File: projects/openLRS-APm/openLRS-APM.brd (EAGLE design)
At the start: 43.3 x 21.8 mm, 23 parts, among them IC2 RFM23BPSMD, J1 AVR_SPI_PRG_6PTH, U1 ATMEGA328P, X2 SMA-142-0711-821/826, Y1 16MHz

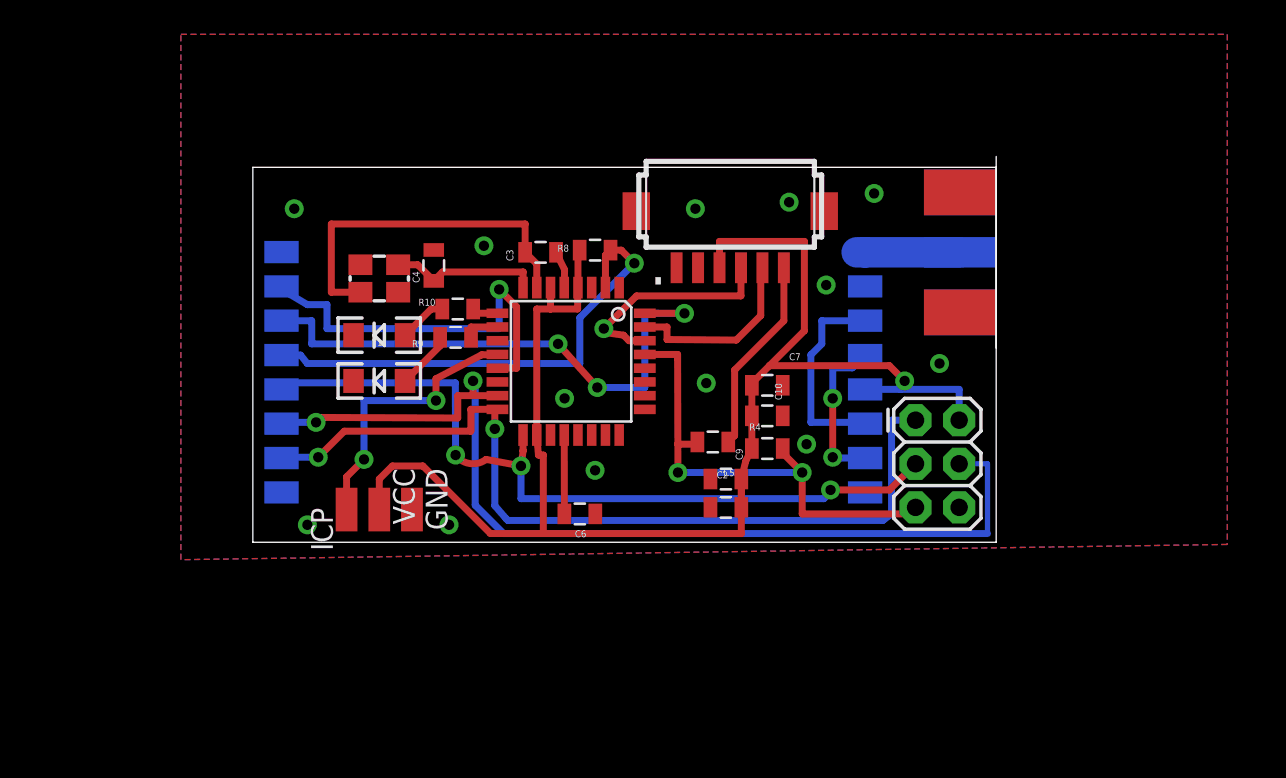
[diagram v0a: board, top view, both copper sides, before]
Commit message: Fixed designs
Ready for first fabrication (I hope). Cleaned and prepared.
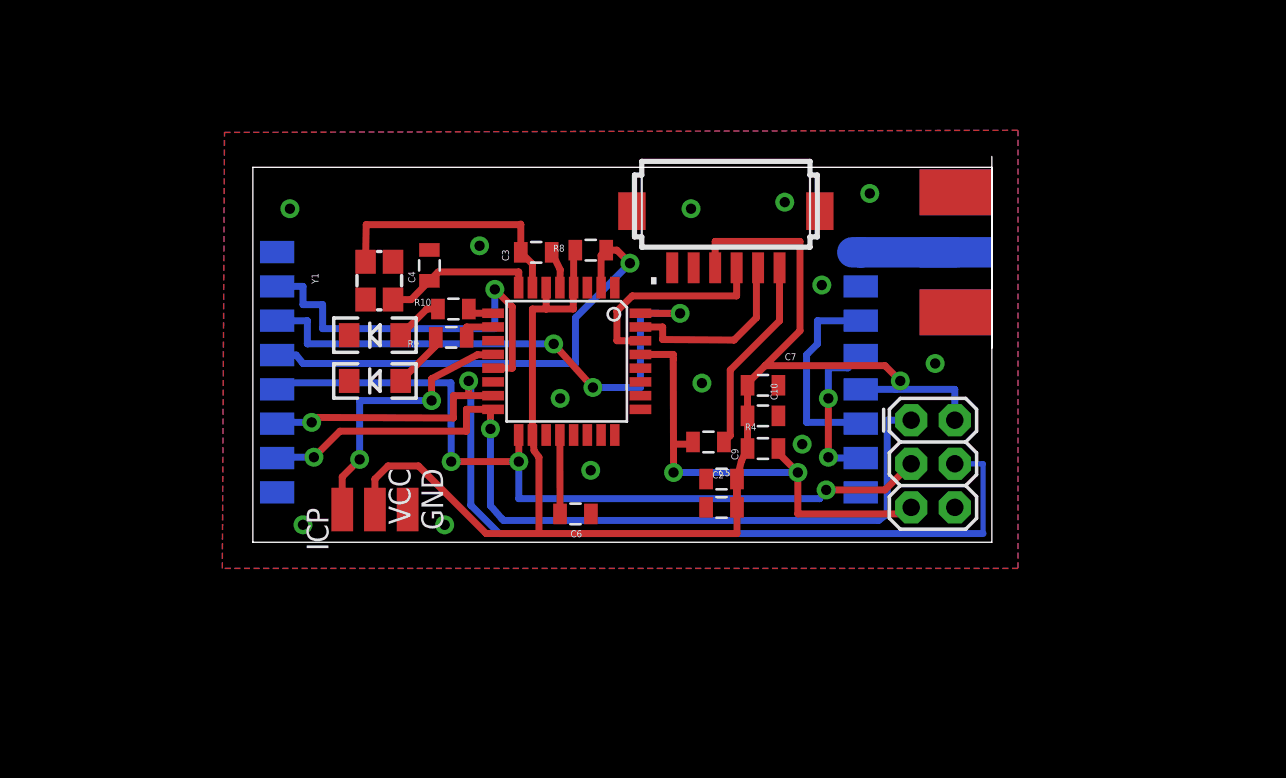
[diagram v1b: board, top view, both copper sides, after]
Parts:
- moved X2 0.25 mm to (43.1, 16.9)
- moved C10 0.25 mm to (29.7, 7.37)
- moved C2 0.25 mm to (27.3, 2.03)
- moved C5 0.25 mm to (26.5, 5.84)
- moved C6 0.25 mm to (18.8, 1.65)
- moved C7 0.25 mm to (29.7, 9.14)
- moved C9 0.25 mm to (27.3, 3.68)
- moved GND 0.25 mm to (9.02, 1.91)
- moved IC2 0.25 mm to (18.4, 9.91)
- moved R10 0.25 mm to (11.7, 13.6)
- moved R4 0.25 mm to (29.7, 5.46)
- moved R8 0.25 mm to (19.7, 17.0)
- moved U1 0.25 mm to (18.3, 10.5)
- moved ICP 0.25 mm to (5.21, 1.91)
- moved C4 0.25 mm to (10.3, 16.1)
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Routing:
- net N$11: track 21.0 -> 15.2 mm
- net RXD: track 13.1 -> 12.1 mm, vias 1 -> 0
- net SDN: track 22.9 -> 23.7 mm
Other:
- board size 43.3 x 21.8 mm -> 43.1 x 21.8 mm

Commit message: Cleaned, Checked, fixed Ground planes
Beefed up Power busses. Fixed the Telemetry Pinout.
Closer to a polished Revision one. Will look into DF-13 PPM signals.
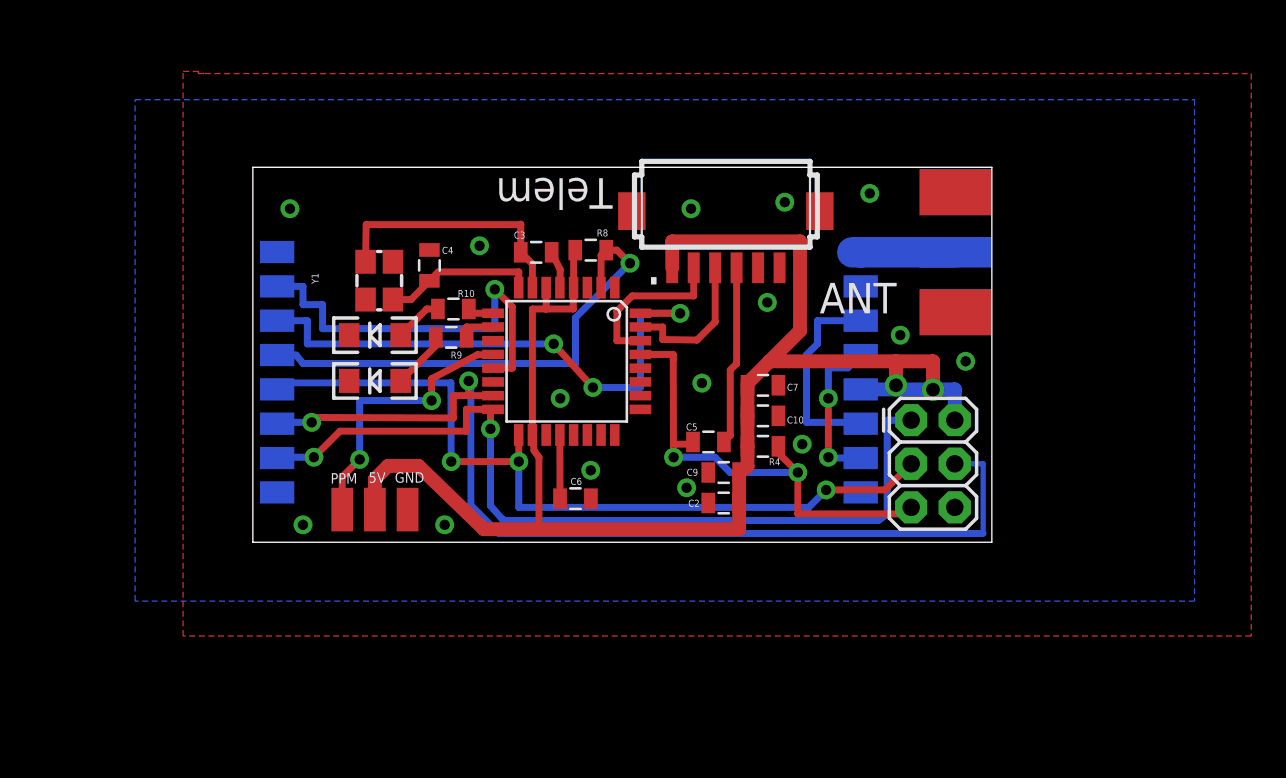
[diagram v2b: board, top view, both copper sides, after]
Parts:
- moved C6 0.89 mm to (18.8, 2.54)
- moved C9 0.40 mm to (27.4, 4.06)
- moved C2 0.28 mm to (27.4, 2.29)
- moved R4 0.13 mm to (29.7, 5.59)
- renumbered ICP to PPM, VCC to 5V
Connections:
- net ICP renamed PPM
- removed net SCL: U1.28
- removed net SDA: U1.27
- removed net VCN: U1.11
- net DTR: now also TELEMETRY.P$4; no longer TELEMETRY.P$6
- net GND: now also TELEMETRY.P$5, TELEMETRY.P$6; no longer TELEMETRY.P$1, TELEMETRY.P$2
- net RXD: now also TELEMETRY.P$2; no longer TELEMETRY.P$4
- net TXD: now also TELEMETRY.P$3; no longer TELEMETRY.P$5
- net VCC: now also TELEMETRY.P$1; no longer TELEMETRY.P$3
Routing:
- net VCC: track 87.8 -> 92.6 mm, vias 1 -> 2
- net RXD: track 12.1 -> 9.58 mm
- net TXD: track 11.0 -> 8.68 mm
- net DTR: track 11.5 -> 10.5 mm
- net N$14: track 4.60 -> 3.71 mm
- net SCK: track 47.0 -> 47.7 mm
- net GND: vias 13 -> 15
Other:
- board text added: "1"
- board text added: "ANT"
- board text added: "Telem"

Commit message: Changed LED's to 0805.
Prototype Soon. all SMDs are 0805. Hope to find SMA connector
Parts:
- LED1, LED2: device SparkFun-LED:LED-1206 -> led:SML0805
- R10, R9: value 220R -> 220
- moved LED2 3.63 mm to (4.19, 9.91), turned to 90 degrees
- moved Y1 2.57 mm to (6.99, 12.7)
- moved LED1 0.80 mm to (7.37, 8.64), turned to 0 degrees
- moved C4 0.54 mm to (10.7, 15.7), turned to 180 degrees
- moved R10 0.13 mm to (11.6, 13.6)
- renumbered 5V to VCC
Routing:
- net GND: track 2.19 -> 12.3 mm
- net N$9: track 2.80 -> 9.75 mm
- net N$12: track 8.92 -> 11.4 mm
- net N$11: track 15.2 -> 13.9 mm
- net N$10: track 3.39 -> 4.09 mm
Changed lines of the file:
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@@
 <attribute name="VALUE" x="29.845" y="4.826" size="0.4064" layer="27" rot="R180"/>
 </element>
-<element name="R9" library="SparkFun-Resistors" package="0805" value="220R" x="11.557" y="11.938" smashed="yes">
+<element name="R9" library="SparkFun-Resistors" package="0805" value="220" x="11.557" y="11.938" smashed="yes">
 <attribute name="NAME" x="12.192" y="11.1125" size="0.4064" layer="25" rot="R180"/>
 <attribute name="VALUE" x="11.2395" y="11.176" size="0.4064" layer="27" rot="R180"/>
 </element>
-<element name="R10" library="SparkFun-Resistors" package="0805" value="220R" x="11.684" y="13.589" smashed="yes">
-<attribute name="NAME" x="11.938" y="14.2875" size="0.4064" layer="25"/>
+<element name="R10" library="SparkFun-Resistors" package="0805" value="220" x="11.557" y="13.589" smashed="yes">
+<attribute name="NAME" x="11.811" y="14.2875" size="0.4064" layer="25"/>
 <attribute name="VALUE" x="10.4775" y="14.351" size="0.4064" layer="27"/>
 </element>
-<element name="LED1" library="SparkFun-LED" package="LED-1206" value="RED" x="7.112" y="9.398" smashed="yes" rot="R180"/>
-<element name="LED2" library="SparkFun-LED" package="LED-1206" value="GRN" x="7.112" y="12.065" smashed="yes" rot="R180"/>
+<element name="LED1" library="led" package="SML0805" value="RED" x="7.366" y="8.636" smashed="yes"/>
+<element name="LED2" library="led" package="SML0805" value="GRN" x="4.191" y="9.906" smashed="yes" rot="R90"/>
 <element name="C3" library="SparkFun-Capacitors" package="0805" value="12pF" x="16.51" y="16.891" smashed="yes">
 <attribute name="NAME" x="15.875" y="18.0975" size="0.4064" layer="25" rot="R180"/>
 <attribute name="VALUE" x="17.526" y="18.161" size="0.4064" layer="27" rot="R180"/>
 </element>
-<element name="C4" library="SparkFun-Capacitors" package="0805" value="12pF" x="10.287" y="16.129" smashed="yes" rot="R90">
-<attribute name="NAME" x="11.684" y="17.2085" size="0.4064" layer="25" rot="R180"/>
-<attribute name="VALUE" x="10.922" y="16.256" size="0.4064" layer="27"/>
-</element>
-<element name="Y1" library="crystal_3225" package="CRYSTAL-SMD-5X3" value="16MHz" x="7.366" y="15.24" smashed="yes" rot="R90">
-<attribute name="NAME" x="3.829" y="15.051" size="0.4064" layer="25" rot="R90"/>
-<attribute name="VALUE" x="5.399" y="16.953" size="0.4064" layer="27" rot="R270"/>
+<element name="C4" library="SparkFun-Capacitors" package="0805" value="12pF" x="10.668" y="15.748" smashed="yes" rot="R180">
+<attribute name="NAME" x="9.398" y="16.5735" size="0.4064" layer="25"/>
+<attribute name="VALUE" x="11.684" y="17.018" size="0.4064" layer="27" rot="R180"/>
+</element>
+<element name="Y1" library="crystal_3225" package="CRYSTAL-SMD-5X3" value="16MHz" x="6.985" y="12.7" smashed="yes" rot="R90">
+<attribute name="NAME" x="5.48" y="11.495" size="0.4064" layer="25" rot="R90"/>
+<attribute name="VALUE" x="5.396" y="12.638" size="0.4064" layer="27" rot="R90"/>
 </element>
 <element name="C9" library="SparkFun-Capacitors" package="0805" value="1uF" x="27.432" y="4.064" smashed="yes" rot="R180">
@@
 <attribute name="NAME" x="6.083" y="4.026" size="0.6096" layer="25" rot="R180"/>
 </element>
-<element name="5V" library="wirepad" package="SMD1,27-2,54" value="" x="7.112" y="1.905" smashed="yes" rot="R180">
+<element name="VCC" library="wirepad" package="SMD1,27-2,54" value="" x="7.112" y="1.905" smashed="yes" rot="R180">
 <attribute name="VALUE" x="7.112" y="1.905" size="0.0254" layer="27" rot="R180"/>
 <attribute name="NAME" x="6.744" y="3.467" size="0.6096" layer="25"/>
@@
 <contactref element="GND" pad="1"/>
 <wire x1="1.415" y1="16.891" x2="1.415" y2="16.906" width="0.2032" layer="16"/>
-<via x="2.159" y="19.431" extent="1-16" drill="0.6"/>
 <via x="19.685" y="4.191" extent="1-16" drill="0.6"/>
 <via x="32.004" y="5.715" extent="1-16" drill="0.6"/>
@@
 <wire x1="17.888" y1="14.8336" x2="17.907" y2="15.875" width="0.4064" layer="1"/>
 <wire x1="17.907" y1="15.875" x2="17.41" y2="16.891" width="0.4064" layer="1"/>
-<via x="13.208" y="17.272" extent="1-16" drill="0.6"/>
 <via x="25.273" y="3.175" extent="1-16" drill="0.6"/>
 <via x="37.719" y="12.065" extent="1-16" drill="0.6"/>
@@
 <contactref element="TELEMETRY" pad="P$6"/>
 <contactref element="TELEMETRY" pad="P$5"/>
+<via x="4.699" y="15.621" extent="1-16" drill="0.6"/>
+<via x="8.128" y="15.494" extent="1-16" drill="0.6"/>
+<wire x1="7.785" y1="13.8" x2="8.128" y2="13.8" width="0.4064" layer="1"/>
+<wire x1="8.128" y1="13.8" x2="8.128" y2="15.494" width="0.4064" layer="1"/>
+<wire x1="6.185" y1="11.6" x2="4.699" y2="13.086" width="0.4064" layer="1"/>
+<wire x1="4.699" y1="13.086" x2="4.699" y2="15.621" width="0.4064" layer="1"/>
+<wire x1="4.699" y1="15.621" x2="4.826" y2="15.494" width="0.4064" layer="16"/>
+<wire x1="4.826" y1="15.494" x2="8.128" y2="15.494" width="0.4064" layer="16"/>
 </signal>
 <signal name="VCC">
@@
 <contactref element="R8" pad="2"/>
 <contactref element="C2" pad="1"/>
-<contactref element="5V" pad="1"/>
+<contactref element="VCC" pad="1"/>
 <wire x1="7.112" y1="1.905" x2="7.112" y2="3.683" width="0.8128" layer="1"/>
 <wire x1="7.112" y1="3.683" x2="7.874" y2="4.445" width="0.8128" layer="1"/>
@@
 <contactref element="R10" pad="2"/>
 <wire x1="13.9954" y1="13.341" x2="12.584" y2="13.341" width="0.4064" layer="1"/>
-<wire x1="12.584" y1="13.341" x2="12.584" y2="13.589" width="0.4064" layer="1"/>
+<wire x1="12.584" y1="13.341" x2="12.457" y2="13.589" width="0.4064" layer="1"/>
 </signal>
 <signal name="N$11">
@@
 <wire x1="16.288" y1="14.8336" x2="16.288" y2="16.213" width="0.4064" layer="1"/>
 <wire x1="16.288" y1="16.213" x2="15.61" y2="16.891" width="0.4064" layer="1"/>
-<wire x1="15.61" y1="16.891" x2="15.61" y2="18.504" width="0.4064" layer="1"/>
-<wire x1="6.604" y1="18.504" x2="6.566" y2="16.34" width="0.4064" layer="1"/>
-<wire x1="15.61" y1="18.542" x2="15.61" y2="18.504" width="0.4064" layer="1"/>
-<wire x1="15.61" y1="18.504" x2="6.604" y2="18.504" width="0.4064" layer="1"/>
+<wire x1="15.61" y1="16.891" x2="7.874" y2="16.891" width="0.4064" layer="1"/>
+<wire x1="7.874" y1="16.891" x2="6.223" y2="15.24" width="0.4064" layer="1"/>
+<wire x1="6.223" y1="15.24" x2="6.223" y2="13.838" width="0.4064" layer="1"/>
+<wire x1="6.223" y1="13.838" x2="6.185" y2="13.8" width="0.4064" layer="1"/>
 </signal>
 <signal name="N$12">
@@
 <contactref element="C4" pad="1"/>
 <contactref element="Y1" pad="1"/>
-<wire x1="10.287" y1="15.229" x2="10.795" y2="15.748" width="0.4064" layer="1"/>
-<wire x1="10.795" y1="15.748" x2="15.494" y2="15.748" width="0.4064" layer="1"/>
-<wire x1="15.494" y1="15.748" x2="15.488" y2="14.8336" width="0.4064" layer="1"/>
-<wire x1="8.166" y1="14.14" x2="9.222" y2="14.135" width="0.4064" layer="1"/>
-<wire x1="9.222" y1="14.135" x2="10.287" y2="15.229" width="0.4064" layer="1"/>
+<wire x1="15.488" y1="14.8336" x2="14.5736" y2="15.748" width="0.4064" layer="1"/>
+<wire x1="14.5736" y1="15.748" x2="11.568" y2="15.748" width="0.4064" layer="1"/>
+<wire x1="11.568" y1="15.748" x2="10.425" y2="14.605" width="0.4064" layer="1"/>
+<wire x1="10.425" y1="14.605" x2="8.89" y2="14.605" width="0.4064" layer="1"/>
+<wire x1="8.89" y1="14.605" x2="8.89" y2="11.938" width="0.4064" layer="1"/>
+<wire x1="8.89" y1="11.938" x2="8.552" y2="11.6" width="0.4064" layer="1"/>
+<wire x1="8.552" y1="11.6" x2="7.785" y2="11.6" width="0.4064" layer="1"/>
 </signal>
 <signal name="N$13">
@@
 <contactref element="R10" pad="1"/>
 <contactref element="LED2" pad="A"/>
-<wire x1="10.784" y1="13.589" x2="10.136" y2="13.589" width="0.4064" layer="1"/>
-<wire x1="10.136" y1="13.589" x2="8.612" y2="12.065" width="0.4064" layer="1"/>
+<wire x1="10.657" y1="13.589" x2="9.652" y2="13.589" width="0.4064" layer="1"/>
+<wire x1="9.652" y1="13.589" x2="9.652" y2="11.557" width="0.4064" layer="1"/>
+<wire x1="9.652" y1="11.557" x2="8.382" y2="9.906" width="0.4064" layer="1"/>
+<wire x1="8.382" y1="9.906" x2="5.241" y2="9.906" width="0.4064" layer="1"/>
+<wire x1="5.241" y1="9.906" x2="4.191" y2="10.956" width="0.4064" layer="1"/>
 </signal>
 <signal name="N$10">
@@
 <contactref element="LED1" pad="A"/>
 <wire x1="10.657" y1="11.938" x2="10.657" y2="11.443" width="0.4064" layer="1"/>
-<wire x1="10.657" y1="11.443" x2="8.612" y2="9.398" width="0.4064" layer="1"/>
+<wire x1="10.657" y1="11.443" x2="8.416" y2="8.636" width="0.4064" layer="1"/>
 </signal>
 <signal name="SDN">
